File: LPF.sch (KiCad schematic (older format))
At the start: 107 parts, among them P1 SMA, P2 J5/J5' Ctrl Brd, P3 SMA, P4 SMA

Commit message: version 1.1
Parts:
- added JP1, JP2, JP3, JP4, JP5, JP6, JP7: Jumper, Jumper:Coax_wire_1.20m_Drill, symbol Jumper
- RL15: value EE2-5NU -> EC2-12NU
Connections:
- net 12/10m: now also JP5.2; no longer C14.1, RL6.12
- net 160m: now also JP7.2; no longer C8.1, RL1.12
- net 17/15m: now also JP4.2; no longer C13.1, RL5.12
- net 30/20m: now also JP3.2; no longer C12.1, RL4.12
- net 40m: now also JP2.2; no longer C10.1, RL3.12
- net 6m_Bypass: now also JP6.2; no longer C15.1, RL7.12
- net 80m: now also JP1.2; no longer C9.1, RL2.12
- new net: C8.1, JP7.1, RL1.12
- new net: C12.1, JP3.1, RL4.12
- new net: C15.1, JP6.1, RL7.12
- new net: C10.1, JP2.1, RL3.12
- new net: C9.1, JP1.1, RL2.12
- new net: C13.1, JP4.1, RL5.12
- new net: C14.1, JP5.1, RL6.12
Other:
- note added: "RX_MASTER_IN"
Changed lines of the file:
@@
 	5200 1950 5200 2000
-Wire Wire Line
-	5150 1650 6500 1650
 Wire Wire Line
 	4450 1650 4550 1650
@@
 	7150 3250 7200 3250
 Wire Wire Line
-	5150 2950 6500 2950
-Wire Wire Line
 	6450 3250 6450 3300
 Wire Wire Line
@@
 	7150 4550 7200 4550
 Wire Wire Line
-	5150 4250 6500 4250
-Wire Wire Line
 	6450 4550 6450 4600
 Wire Wire Line
@@
 	7150 5850 7250 5850
 Wire Wire Line
-	5150 5550 6500 5550
-Wire Wire Line
 	6450 5850 6450 5900
 Wire Wire Line
@@
 	7150 9800 7150 9850
 Wire Wire Line
-	5150 9500 6500 9500
-Wire Wire Line
 	6450 9800 6450 9850
 Wire Wire Line
@@
 	7200 7200 7150 7200
 Wire Wire Line
-	5150 6850 6500 6850
-Wire Wire Line
 	6450 7150 6450 7200
 Wire Wire Line
@@
 Wire Wire Line
 	7150 8500 7200 8500
-Wire Wire Line
-	5150 8200 6500 8200
 Wire Wire Line
 	6450 8500 6450 8550
@@
 P 3700 5000
 F 0 "RL15" V 4450 4950 50  0000 L CNN
-F 1 "EE2-5NU" V 3700 4850 50  0000 L CNN
+F 1 "EC2-12NU" V 3700 4850 50  0000 L CNN
 F 2 "2_Form_C_Relay:THT_2_formC" H 3700 5000 50  0001 C CNN
 F 3 "" H 3700 5000 50  0001 C CNN
@@
 Text GLabel 4100 5200 3    60   Input ~ 0
 TX_RX_RLY
-Text Notes 1150 4950 0    79   ~ 16
+Text Notes 1150 4950 0    39   ~ 0
 To RX Conn Brd\n
-Text Notes 1000 4400 0    79   ~ 16
+Text Notes 1350 4450 0    39   ~ 0
 To 15 W PA output\n
 Text Notes 7650 3800 1    79   ~ 16
@@
 Wire Wire Line
 	2800 2600 2800 2650
+Text Notes 1250 4800 0    79   ~ 16
+RX_MASTER_IN
+Text Notes 1450 4300 0    79   ~ 16
+HF_TX
+$Comp
+L Jumper JP1
+U 1 1 5946D769
+P 5550 2950
+F 0 "JP1" H 5550 3100 50  0000 C CNN
+F 1 "Jumper" H 5550 2870 50  0000 C CNN
+F 2 "Jumper:Coax_wire_1.20m_Drill" H 5550 2950 50  0001 C CNN
+F 3 "" H 5550 2950 50  0001 C CNN
+	1    5550 2950
+	1    0    0    -1
+$EndComp
+$Comp
+L Jumper JP7
+U 1 1 5946F7F4
+P 5750 1650
+F 0 "JP7" H 5750 1800 50  0000 C CNN
+F 1 "Jumper" H 5750 1570 50  0000 C CNN
+F 2 "Jumper:Coax_wire_1.20m_Drill" H 5750 1650 50  0001 C CNN
+F 3 "" H 5750 1650 50  0001 C CNN
+	1    5750 1650
+	1    0    0    -1
+$EndComp
+Wire Wire Line
+	5150 1650 5450 1650
+Wire Wire Line
+	6050 1650 6500 1650
+$Comp
+L Jumper JP2
+U 1 1 59472F9F
+P 5550 4250
+F 0 "JP2" H 5550 4400 50  0000 C CNN
+F 1 "Jumper" H 5550 4170 50  0000 C CNN
+F 2 "Jumper:Coax_wire_1.20m_Drill" H 5550 4250 50  0001 C CNN
+F 3 "" H 5550 4250 50  0001 C CNN
+	1    5550 4250
+	1    0    0    -1
+$EndComp
+$Comp
+L Jumper JP3
+U 1 1 59473567
+P 5550 5550
+F 0 "JP3" H 5550 5700 50  0000 C CNN
+F 1 "Jumper" H 5550 5470 50  0000 C CNN
+F 2 "Jumper:Coax_wire_1.20m_Drill" H 5550 5550 50  0001 C CNN
+F 3 "" H 5550 5550 50  0001 C CNN
+	1    5550 5550
+	1    0    0    -1
+$EndComp
+$Comp
+L Jumper JP4
+U 1 1 5947360C
+P 5550 6850
+F 0 "JP4" H 5550 7000 50  0000 C CNN
+F 1 "Jumper" H 5550 6770 50  0000 C CNN
+F 2 "Jumper:Coax_wire_1.20m_Drill" H 5550 6850 50  0001 C CNN
+F 3 "" H 5550 6850 50  0001 C CNN
+	1    5550 6850
+	1    0    0    -1
+$EndComp
+$Comp
+L Jumper JP5
+U 1 1 59473A3C
+P 5550 8200
+F 0 "JP5" H 5550 8350 50  0000 C CNN
+F 1 "Jumper" H 5550 8120 50  0000 C CNN
+F 2 "Jumper:Coax_wire_1.20m_Drill" H 5550 8200 50  0001 C CNN
+F 3 "" H 5550 8200 50  0001 C CNN
+	1    5550 8200
+	1    0    0    -1
+$EndComp
+$Comp
+L Jumper JP6
+U 1 1 59473AE3
+P 5550 9500
+F 0 "JP6" H 5550 9650 50  0000 C CNN
+F 1 "Jumper" H 5550 9420 50  0000 C CNN
+F 2 "Jumper:Coax_wire_1.20m_Drill" H 5550 9500 50  0001 C CNN
+F 3 "" H 5550 9500 50  0001 C CNN
+	1    5550 9500
+	1    0    0    -1
+$EndComp
+Wire Wire Line
+	5150 6850 5250 6850
+Wire Wire Line
+	5850 6850 6500 6850
+Wire Wire Line
+	5150 9500 5250 9500
+Wire Wire Line
+	5850 9500 6500 9500
+Wire Wire Line
+	5850 8200 6500 8200
+Wire Wire Line
+	5150 8200 5250 8200
+Wire Wire Line
+	5150 5550 5250 5550
+Wire Wire Line
+	5850 5550 6500 5550
+Wire Wire Line
+	5150 4250 5250 4250
+Wire Wire Line
+	5850 4250 6500 4250
+Wire Wire Line
+	5150 2950 5250 2950
+Wire Wire Line
+	5850 2950 6500 2950
 $EndSCHEMATC

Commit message: minor changes, adding kk lib, still under dev.
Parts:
- removed RL1, RL10, RL11, RL12, RL13, RL14, RL15, RL2, RL3, RL4, RL5, RL6, RL7, RL8, RL9: EC2-12NU, 2_Form_C_Relay:THT_2_formC, symbol EE2-5NU
- added RL1, RL10, RL11, RL12, RL13, RL14, RL15, RL2, RL3, RL4, RL5, RL6, RL7, RL8, RL9: D2n, symbol D2n
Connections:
- net +12V: now also RL1.1, RL10.1, RL11.1, RL12.1, RL13.1, RL14.1, RL15.1, RL2.1, RL3.1, RL4.1, RL5.1, RL6.1, RL7.1, RL8.1, RL9.1
- net 12/10m: now also RL14.16
- net 160m: now also RL9.16
- net 17/15m: now also RL13.16
- net 30/20m: now also RL12.16
- net 40m: now also RL11.16
- net 6m_Bypass: now also RL15.16
- net 80m: now also RL10.16
- net GND: now also RL10.11, RL10.6, RL11.11, RL11.6, RL12.11, RL12.6, RL13.11, RL13.6, RL14.11, RL14.6, RL15.11, RL15.6, RL2.11, RL2.6, RL3.11, RL3.6, RL4.11, RL4.6, RL5.11, RL5.6, RL6.11, RL6.6, RL7.11, RL7.6, RL8.11, RL8.6, RL9.11, RL9.6
- net TX_RX_RLY: now also RL1.16
- net at P3.1 (In): now also RL10.8, RL10.9, RL11.8, RL11.9, RL12.8, RL12.9, RL13.8, RL13.9, RL14.8, RL14.9, RL15.8, RL15.9, RL9.8, RL9.9
- net at C8.1, JP7.1: now also RL2.16
- net at C19.2, C25.1, L3.1: now also RL2.13, RL2.4
- net at C39.2, C46.2, L10.2: now also RL9.13, RL9.4
- net at C40.2, C47.2, L11.2: now also RL10.13, RL10.4
- net at C20.2, C26.1, L4.1: now also RL3.13, RL3.4
- net at C41.2, C48.2, L12.2: now also RL11.13, RL11.4
- net at C21.2, C27.1, L5.1: now also RL4.13, RL4.4
- net at C51.2, C55.2, L16.2: now also RL12.13, RL12.4
- net at C45.2, L15.2: now also RL15.13, RL15.4
- net at C43.2, C49.2, L13.2: now also RL13.13, RL13.4
- net at C22.2, C28.1, L6.1: now also RL6.13, RL6.4
- net at C44.2, C50.2, L14.2: now also RL14.13, RL14.4
- net at C23.2, C29.1, L7.1: now also RL7.13, RL7.4
- net at C17.1, L2.1: now also RL8.13, RL8.4
- net at C11.2, C16.1, L1.1: now also RL5.13, RL5.4
- net at C12.1, JP3.1: now also RL5.16
- net at C15.1, JP6.1: now also RL8.16
- net at C10.1, JP2.1: now also RL4.16
- net at C9.1, JP1.1: now also RL3.16
- net at C13.1, JP4.1: now also RL6.16
- net at C14.1, JP5.1: now also RL7.16
- net at P1.1 (In): now also RL1.8, RL1.9
- net at P4.1 (In): now also RL1.11, RL1.6
- new net: RL1.13, RL1.4, RL2.8, RL2.9, RL3.8, RL3.9, RL4.8, RL4.9, RL5.8, RL5.9, RL6.8, RL6.9, RL7.8, RL7.9, RL8.8, RL8.9

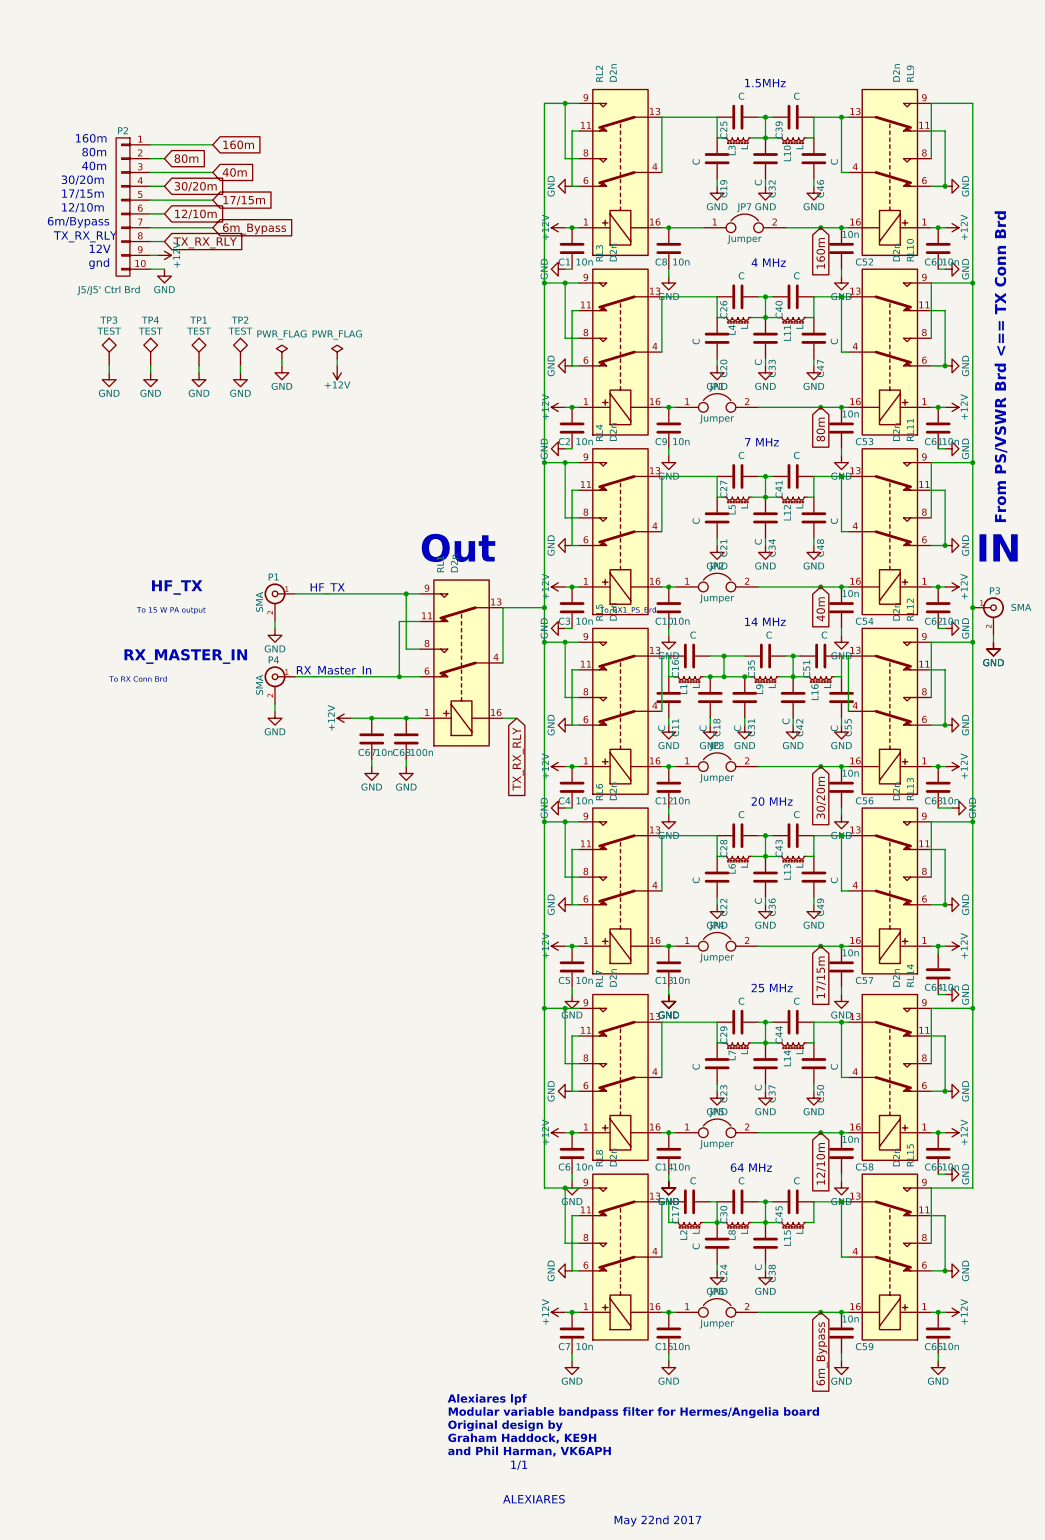
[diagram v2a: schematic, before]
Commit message: new 4 layers routing, mods in schematic
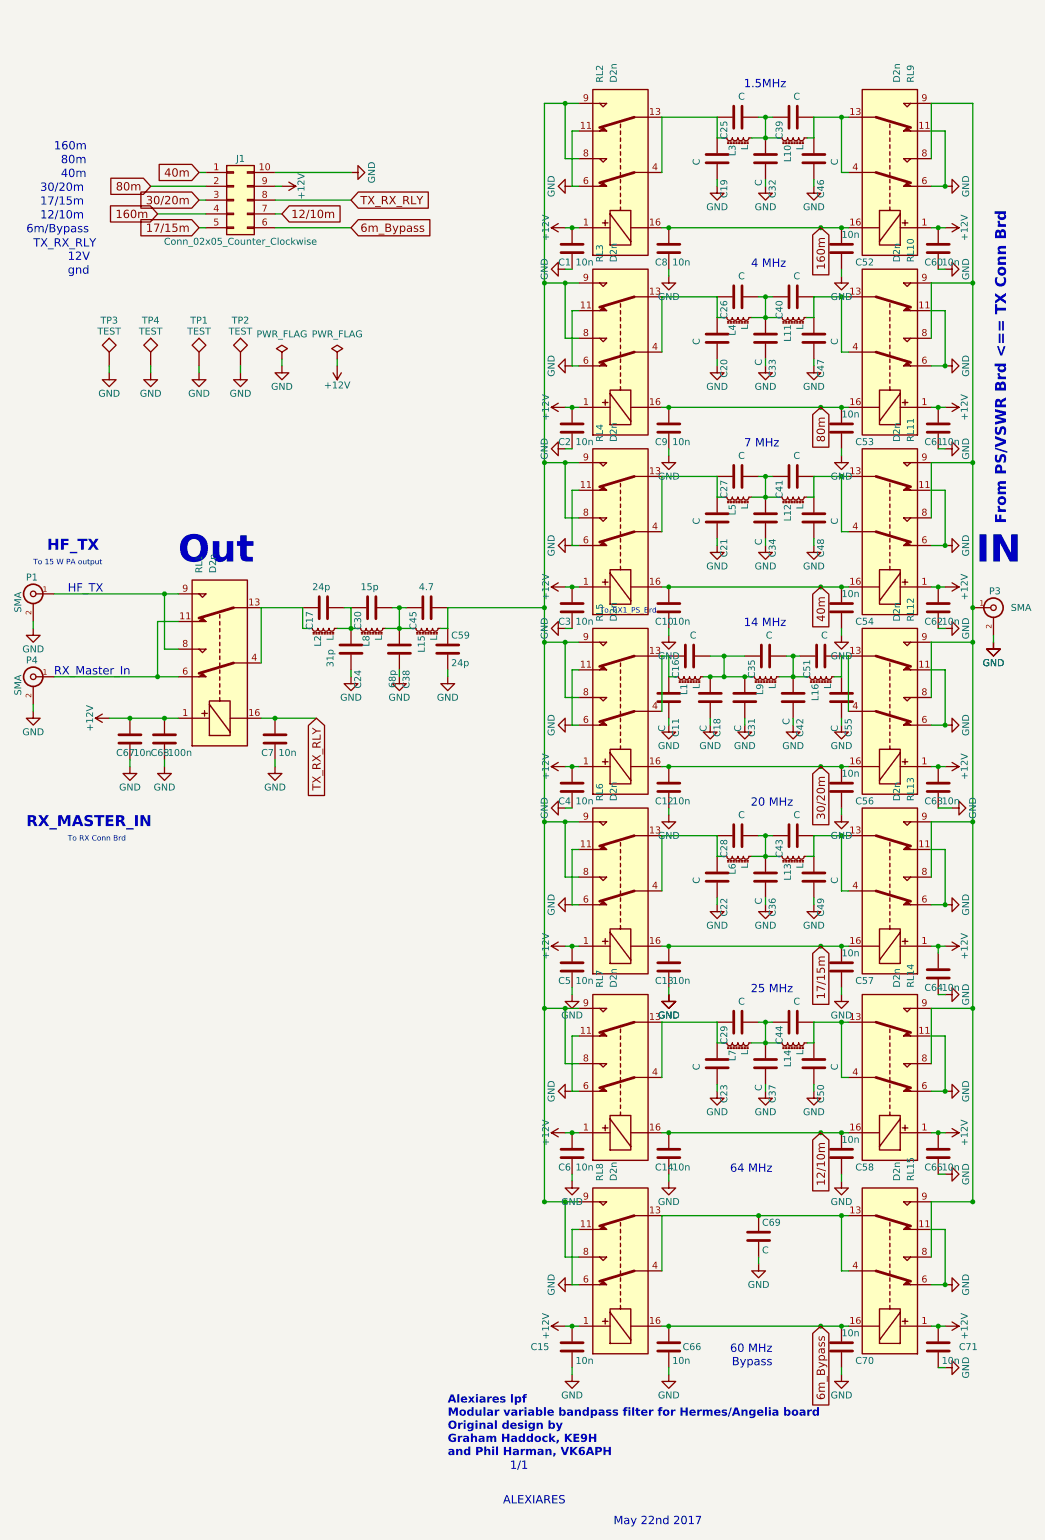
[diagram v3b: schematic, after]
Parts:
- removed JP1, JP2, JP3, JP4, JP5, JP6, JP7: Jumper, Jumper:Coax_wire_1.20m_Drill, symbol Jumper
- removed P2: J5/J5' Ctrl Brd, conn_kk100:kk100_22-23-2101, symbol CONN_01X10
- added C69: C, ATC_B:ATC_500_HandSoldering, symbol C
- added C70, C71: 10n, Capacitors_SMD:C_0805_HandSoldering, symbol C
- added J1: Conn_02x05_Counter_Clockwise, Connectors:IDC_Header_Straight_10pins, symbol Conn_02x05_Counter_Clockwise
- C11, C16, C18, C19, C20, C21, C22, C23, C25, C26, C27, C28, C29, C31, C32, C33, C34, C35, C36, C37, C39, C40, C41, C42, C43, C44, C46, C47, C48, C49, C50, C51, C55: footprint Capacitors_SMD:C_0805_HandSoldering -> Capacitors_SMD:C_1210_HandSoldering
- C17: value C -> 24p; footprint Capacitors_SMD:C_0805_HandSoldering -> Capacitors_SMD:C_1210_HandSoldering
- C24: value C -> 31p; footprint Capacitors_SMD:C_0805_HandSoldering -> Capacitors_SMD:C_1210_HandSoldering
- C30: value C -> 15p; footprint Capacitors_SMD:C_0805_HandSoldering -> Capacitors_SMD:C_1210_HandSoldering
- C38: value C -> 68p; footprint Capacitors_SMD:C_0805_HandSoldering -> Capacitors_SMD:C_1210_HandSoldering
- C45: value C -> 4.7; footprint Capacitors_SMD:C_0805_HandSoldering -> Capacitors_SMD:C_1210_HandSoldering
- C59: value 10n -> 24p; footprint Capacitors_SMD:C_0805_HandSoldering -> Capacitors_SMD:C_1210_HandSoldering
- L1, L10, L11, L12, L13, L14, L15, L16, L2, L3, L4, L5, L6, L7, L8, L9: footprint T50_V_cms:T50_V_smd -> T50:T50_V_THT
- RL1, RL10, RL11, RL12, RL13, RL14, RL15, RL2, RL3, RL4, RL5, RL6, RL7, RL8, RL9: footprint (none) -> 2_Form_C_Relay:D2n
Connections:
- net +12V: now also C15.1, C71.1, J1.9 (Pin_9); no longer C66.1, C7.1
- net 12/10m: now also C14.1, RL7.16, J1.7 (Pin_7)
- net 160m: now also C8.1, RL2.16, J1.4 (Pin_4)
- net 17/15m: now also C13.1, RL6.16, J1.5 (Pin_5)
- net 30/20m: now also C12.1, RL5.16, J1.3 (Pin_3)
- net 40m: now also C10.1, RL4.16, J1.1 (Pin_1)
- net 6m_Bypass: now also C66.1, RL8.16, C70.2, J1.6 (Pin_6); no longer C59.2
- net 80m: now also C9.1, RL3.16, J1.2 (Pin_2)
- net GND: now also C59.2, C69.2, C70.1, C71.2, J1.10 (Pin_10); no longer C59.1
- net TX_RX_RLY: now also C7.1, J1.8 (Pin_8)
- net at C45.2, L15.2: now also C59.1, RL2.8, RL2.9, RL3.8, RL3.9, RL4.8, RL4.9, RL5.8, RL5.9, RL6.8, RL6.9, RL7.8, RL7.9, RL8.8, RL8.9; no longer RL15.13, RL15.4
- net at C17.1, L2.1: now also RL1.13, RL1.4; no longer RL8.13, RL8.4
- new net: C69.1, RL15.13, RL15.4, RL8.13, RL8.4
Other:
- note added: "60 MHz\nBypass\n"
- moved on the sheet: C17, C24, C30, C38, C45, C67, C68, L15, L2, L8, P1, P4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

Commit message: decoupling & freewheeling routing
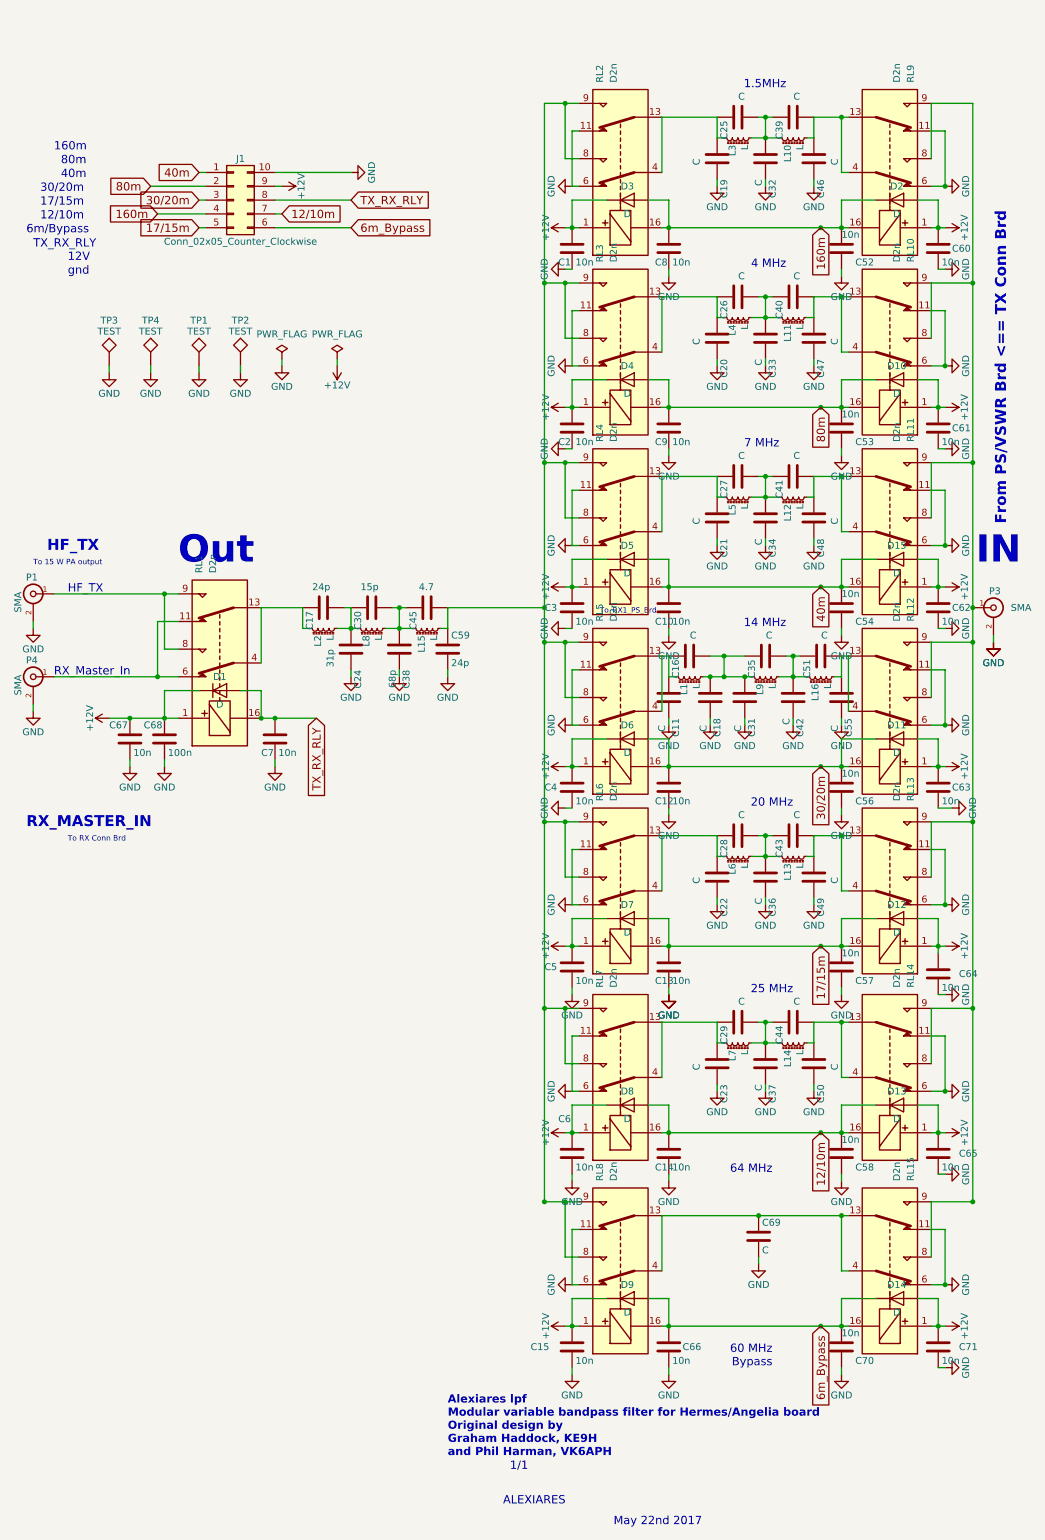
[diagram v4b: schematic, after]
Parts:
- added D1, D10, D11, D12, D13, D14, D15, D2, D3, D4, D5, D6, D7, D8, D9: D, Diodes_SMD:D_SMB, symbol D
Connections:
- net +12V: now also D1.1 (K), D10.2 (A), D11.2 (A), D12.2 (A), D13.2 (A), D14.2 (A), D15.2 (A), D2.2 (A), D3.1 (K), D4.1 (K), D5.1 (K), D6.1 (K), D7.1 (K), D8.1 (K), D9.1 (K)
- net 12/10m: now also D13.1 (K), D8.2 (A)
- net 160m: now also D2.1 (K), D3.2 (A)
- net 17/15m: now also D12.1 (K), D7.2 (A)
- net 30/20m: now also D11.1 (K), D6.2 (A)
- net 40m: now also D15.1 (K), D5.2 (A)
- net 6m_Bypass: now also D14.1 (K), D9.2 (A)
- net 80m: now also D10.1 (K), D4.2 (A)
- net TX_RX_RLY: now also D1.2 (A)

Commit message: RTM
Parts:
- removed C71: 10n, Capacitors_SMD:C_0805_HandSoldering, symbol C
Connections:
- net +12V: now also C10.1, C12.1, C13.1, C14.1, C66.1, C8.1, C9.1, D10.1 (K), D11.1 (K), D12.1 (K), D13.1 (K), D14.1 (K), D15.1 (K), D2.1 (K), RL2.16, RL3.16, RL4.16, RL5.16, RL6.16, RL7.16, RL8.16; no longer C1.1, C15.1, C2.1, C3.1, C4.1, C5.1, C6.1, D10.2 (A), D11.2 (A), D12.2 (A), D13.2 (A), D14.2 (A), D15.2 (A), D2.2 (A), RL2.1, RL3.1, RL4.1, RL5.1, RL6.1, RL7.1, RL8.1
- net 12/10m: now also C6.1, D13.2 (A), RL7.1; no longer C14.1, D13.1 (K), RL7.16
- net 160m: now also C1.1, D2.2 (A), RL2.1; no longer C8.1, D2.1 (K), RL2.16
- net 17/15m: now also C5.1, D12.2 (A), RL6.1; no longer C13.1, D12.1 (K), RL6.16
- net 30/20m: now also C4.1, D11.2 (A), RL5.1; no longer C12.1, D11.1 (K), RL5.16
- net 40m: now also C3.1, D15.2 (A), RL4.1; no longer C10.1, D15.1 (K), RL4.16
- net 6m_Bypass: now also C15.1, D14.2 (A), RL8.1; no longer C66.1, D14.1 (K), RL8.16
- net 80m: now also C2.1, D10.2 (A), RL3.1; no longer C9.1, D10.1 (K), RL3.16
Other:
- moved on the sheet: D3

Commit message: RTM 2, silk corrected, via added, jpg image and readme added
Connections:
- net 6m_Bypass: now also J1.8 (Pin_8); no longer J1.6 (Pin_6)
- net TX_RX_RLY: now also J1.6 (Pin_6); no longer J1.8 (Pin_8)
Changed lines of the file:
@@
 Text Notes 850  2000 0    60   ~ 0
 gnd\n
-Text GLabel 2900 1650 2    60   Input ~ 0
+Text GLabel 2900 1450 2    60   Input ~ 0
 6m_Bypass
 Text GLabel 2400 1550 2    60   Input ~ 0
@@
 Text Notes 750  4900 0    60   ~ 0
 RX_Master_In
-Text GLabel 2900 1450 2    60   Input ~ 0
+Text GLabel 2900 1650 2    60   Input ~ 0
 TX_RX_RLY
 Text GLabel 2650 5200 3    60   Input ~ 0
